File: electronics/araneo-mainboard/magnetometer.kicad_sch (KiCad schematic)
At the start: 1 part, among them IC2 MMC5983MA

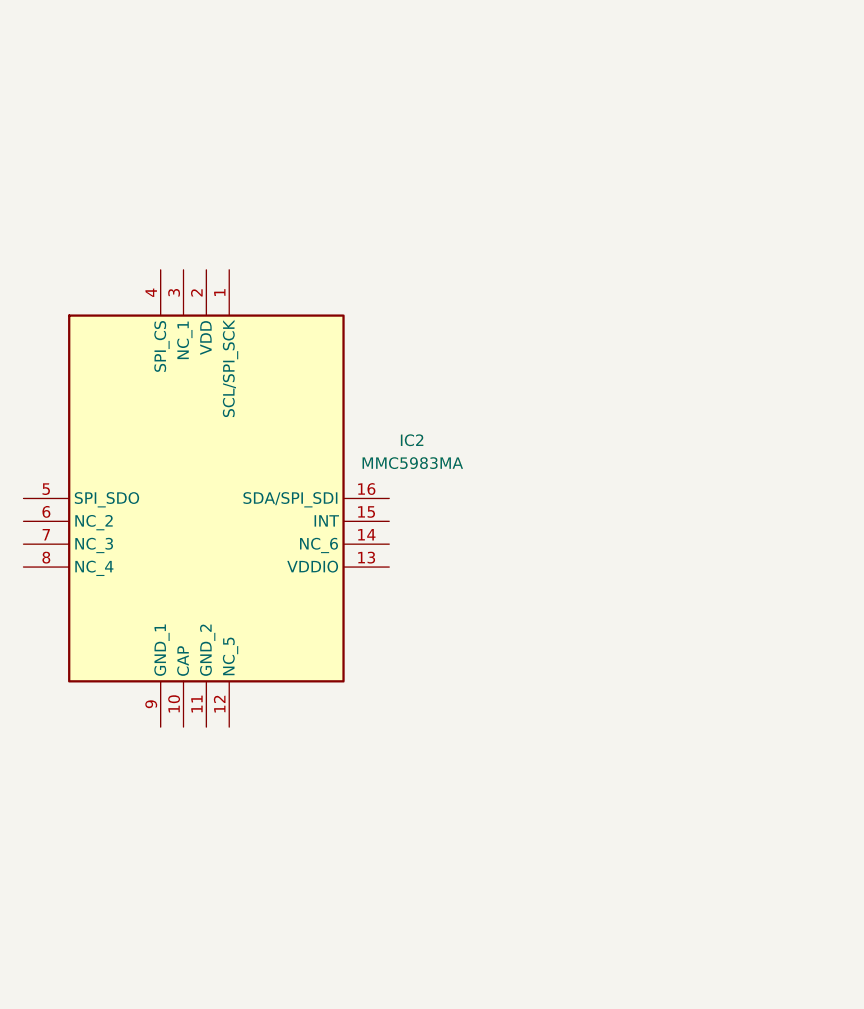
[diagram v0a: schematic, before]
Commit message: add components schematics
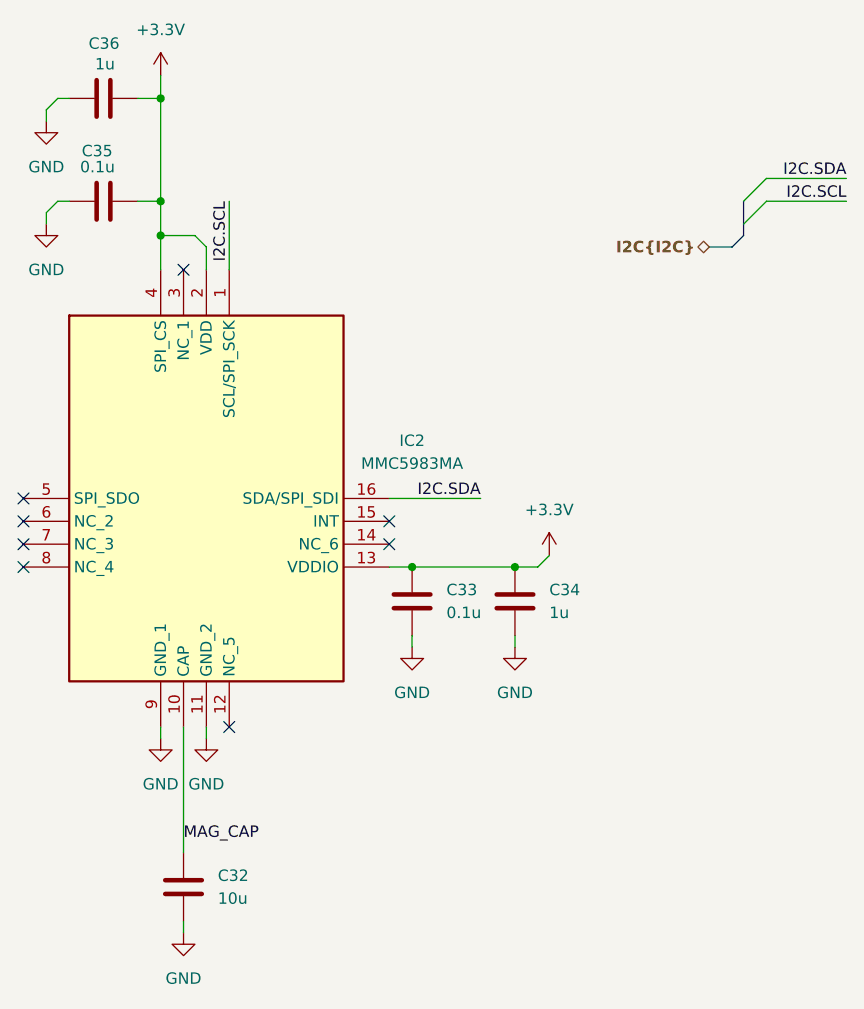
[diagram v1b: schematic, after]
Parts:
- added C32: 10u, symbol Device:C
- added C33, C35: 0.1u, symbol Device:C
- added C34, C36: 1u, symbol Device:C
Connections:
- net I2C.SCL: now reaches IC2.1 (SCL/SPI_SCK)
- net MAG_CAP: now reaches IC2.10 (CAP)
- net MAG_CAP: now also C32.1
- net GND: now reaches IC2.11 (GND_2)
- net GND: now also IC2.9 (GND_1), C32.2, C33.2, C34.2, C35.1, C36.1
- net +3.3V: now reaches IC2.13 (VDDIO)
- net +3.3V: now also IC2.2 (VDD), IC2.4 (SPI_CS), C33.1, C34.1, C35.2, C36.2
- net I2C.SDA: now reaches IC2.16 (SDA/SPI_SDI)
- no-connect marks 0 -> 8

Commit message: electronics: assign footprints
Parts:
- C32: footprint (none) -> PCM_JLCPCB:C_0603
- C33, C34, C35, C36: footprint (none) -> PCM_JLCPCB:C_0402
- IC2: footprint MMC5983MA -> Custom:MMC5983MA
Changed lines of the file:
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@@
 			)
 		)
-		(property "Footprint" ""
+		(property "Footprint" "PCM_JLCPCB:C_0402"
 			(at 133.35 47.2948 0)
 			(hide yes)
@@
 			)
 		)
-		(property "Footprint" ""
+		(property "Footprint" "PCM_JLCPCB:C_0402"
 			(at 133.35 58.7248 0)
 			(hide yes)
@@
 			)
 		)
-		(property "Footprint" ""
+		(property "Footprint" "PCM_JLCPCB:C_0603"
 			(at 139.3952 139.7 0)
 			(hide yes)
@@
 			)
 		)
-		(property "Footprint" "MMC5983MA"
+		(property "Footprint" "Custom:MMC5983MA"
 			(at 157.48 169.85 0)
 			(hide yes)
@@
 			)
 		)
-		(property "Footprint" ""
+		(property "Footprint" "PCM_JLCPCB:C_0402"
 			(at 176.2252 107.95 0)
 			(hide yes)
@@
 			)
 		)
-		(property "Footprint" ""
+		(property "Footprint" "PCM_JLCPCB:C_0402"
 			(at 164.7952 107.95 0)
 			(hide yes)

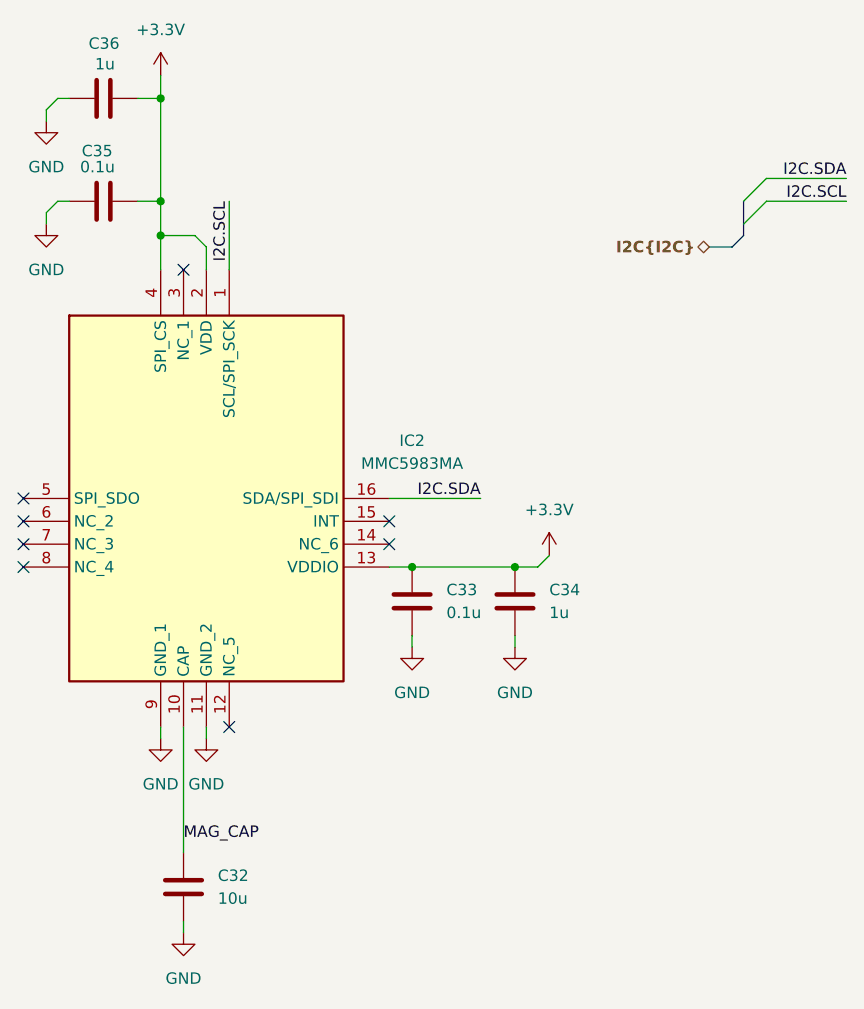
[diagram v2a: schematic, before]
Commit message: add missing components
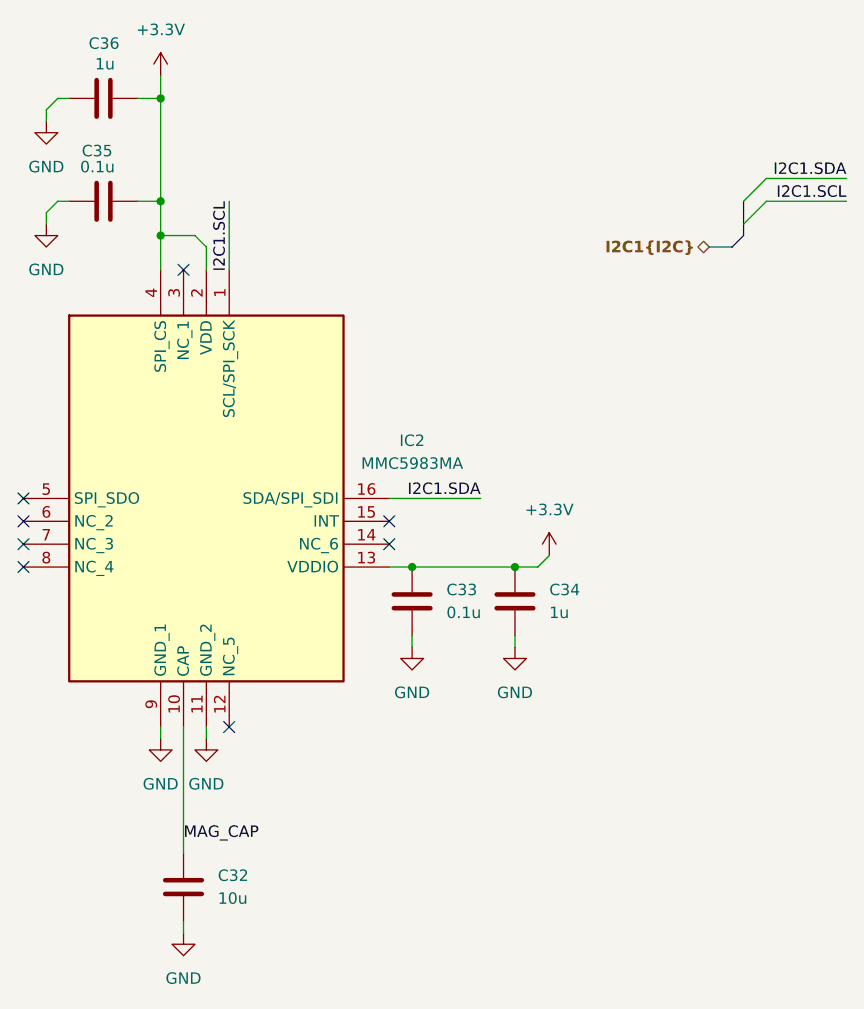
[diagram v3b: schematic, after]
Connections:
- net I2C.SCL renamed I2C1.SCL
- net I2C.SDA renamed I2C1.SDA
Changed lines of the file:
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@@
 		)
 	)
-	(label "I2C.SCL"
+	(label "I2C1.SCL"
 		(at 143.51 59.69 270)
 		(effects
@@
 		)
 	)
-	(label "I2C.SCL"
+	(label "I2C1.SCL"
 		(at 212.09 59.69 180)
 		(effects
@@
 		)
 	)
-	(label "I2C.SDA"
+	(label "I2C1.SDA"
 		(at 171.45 92.71 180)
 		(effects
@@
 		)
 	)
-	(label "I2C.SDA"
+	(label "I2C1.SDA"
 		(at 212.09 57.15 180)
 		(effects
@@
 		)
 	)
-	(hierarchical_label "I2C{I2C}"
+	(hierarchical_label "I2C1{I2C}"
 		(shape bidirectional)
 		(at 196.85 64.77 180)

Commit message: improve schematic and layout, add LCSC parts
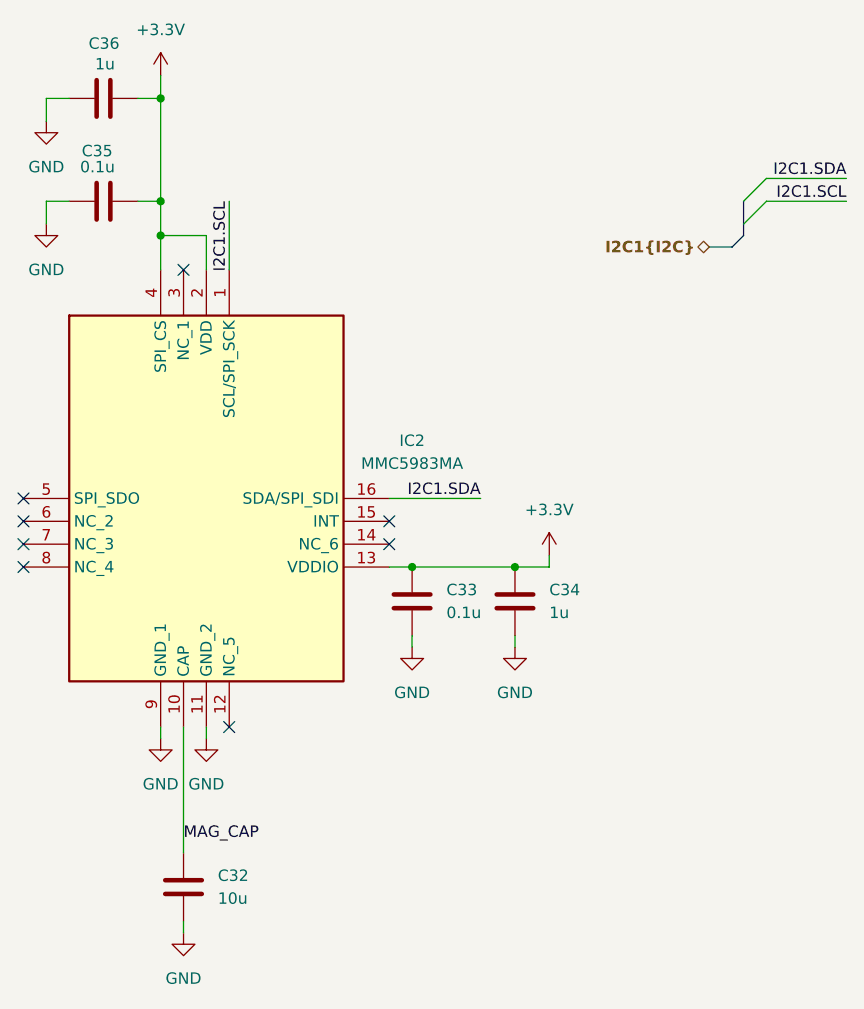
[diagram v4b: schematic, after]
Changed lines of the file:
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@@
 	(wire
 		(pts
-			(xy 175.26 100.33) (xy 177.8 100.33)
+			(xy 175.26 100.33) (xy 179.07 100.33)
 		)
 		(stroke
@@
 	(wire
 		(pts
-			(xy 123.19 60.96) (xy 123.19 62.23)
-		)
-		(stroke
-			(width 0)
-			(type default)
-		)
-	)
-	(wire
-		(pts
 			(xy 140.97 118.11) (xy 140.97 119.38)
 		)
@@
 	(wire
 		(pts
-			(xy 124.46 59.69) (xy 125.73 59.69)
+			(xy 123.19 59.69) (xy 125.73 59.69)
 		)
 		(stroke
@@
 	(wire
 		(pts
+			(xy 123.19 48.26) (xy 125.73 48.26)
+		)
+		(stroke
+			(width 0)
+			(type default)
+		)
+	)
+	(wire
+		(pts
 			(xy 143.51 59.69) (xy 143.51 67.31)
 		)
@@
 	(wire
 		(pts
+			(xy 123.19 48.26) (xy 123.19 50.8)
+		)
+		(stroke
+			(width 0)
+			(type default)
+		)
+	)
+	(wire
+		(pts
 			(xy 163.83 100.33) (xy 175.26 100.33)
 		)
@@
 	(wire
 		(pts
-			(xy 135.89 63.5) (xy 139.7 63.5)
-		)
-		(stroke
-			(width 0)
-			(type default)
-		)
-	)
-	(wire
-		(pts
-			(xy 140.97 64.77) (xy 139.7 63.5)
-		)
-		(stroke
-			(width 0)
-			(type default)
-		)
-	)
-	(wire
-		(pts
-			(xy 140.97 64.77) (xy 140.97 67.31)
-		)
-		(stroke
-			(width 0)
-			(type default)
-		)
-	)
-	(wire
-		(pts
-			(xy 123.19 49.53) (xy 124.46 48.26)
+			(xy 135.89 63.5) (xy 140.97 63.5)
 		)
 		(stroke
@@
 	(wire
 		(pts
+			(xy 140.97 63.5) (xy 140.97 67.31)
+		)
+		(stroke
+			(width 0)
+			(type default)
+		)
+	)
+	(wire
+		(pts
 			(xy 138.43 118.11) (xy 138.43 132.08)
 		)
@@
 	(wire
 		(pts
-			(xy 123.19 60.96) (xy 124.46 59.69)
-		)
-		(stroke
-			(width 0)
-			(type default)
-		)
-	)
-	(wire
-		(pts
 			(xy 135.89 45.72) (xy 135.89 48.26)
 		)
@@
 	(wire
 		(pts
-			(xy 123.19 49.53) (xy 123.19 50.8)
-		)
-		(stroke
-			(width 0)
-			(type default)
-		)
-	)
-	(wire
-		(pts
-			(xy 179.07 99.06) (xy 177.8 100.33)
-		)
-		(stroke
-			(width 0)
-			(type default)
-		)
-	)
-	(wire
-		(pts
-			(xy 124.46 48.26) (xy 125.73 48.26)
+			(xy 179.07 99.06) (xy 179.07 100.33)
 		)
 		(stroke
@@
 		)
 		(stroke
+			(width 0)
+			(type default)
+		)
+	)
+	(wire
+		(pts
+			(xy 123.19 59.69) (xy 123.19 62.23)
+		)
+		(stroke
